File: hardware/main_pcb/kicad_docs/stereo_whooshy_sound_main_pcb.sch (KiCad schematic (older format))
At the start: 4 parts, among them J10 audio_in_B, J11 audio_out_A, J12 audio_out_B, J9 audio_in_A

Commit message: progress on schemo
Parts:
- removed J10: audio_in_B, Connector_PinHeader_2.54mm:PinHeader_1x02_P2.54mm_Vertical, symbol Connector_Generic:Conn_01x02
- removed J11: audio_out_A, Connector_PinHeader_2.54mm:PinHeader_1x02_P2.54mm_Vertical, symbol Connector_Generic:Conn_01x02
- removed J12: audio_out_B, Connector_PinHeader_2.54mm:PinHeader_1x02_P2.54mm_Vertical, symbol Connector_Generic:Conn_01x02
- removed J9: audio_in_A, Connector_PinHeader_2.54mm:PinHeader_1x02_P2.54mm_Vertical, symbol Connector_Generic:Conn_01x02
- added J10: IO_B, Connector_PinHeader_2.54mm:PinHeader_1x03_P2.54mm_Vertical, symbol Connector_Generic:Conn_01x03
- added J9: IO_A, Connector_PinHeader_2.54mm:PinHeader_1x03_P2.54mm_Vertical, symbol Connector_Generic:Conn_01x03
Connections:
- new net audio_in_A: J9.1 (Pin_1)
- new net audio_in_B: J10.1 (Pin_1)
- new net audio_out_A: J9.2 (Pin_2)
- new net audio_out_B: J10.2 (Pin_2)
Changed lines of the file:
@@
 $EndSheet
 $Comp
-L Connector_Generic:Conn_01x02 J9
-U 1 1 5FB8912F
-P 750 1650
-F 0 "J9" H 668 1867 50  0000 C CNN
-F 1 "audio_in_A" H 668 1776 50  0000 C CNN
-F 2 "Connector_PinHeader_2.54mm:PinHeader_1x02_P2.54mm_Vertical" H 750 1650 50  0001 C CNN
-F 3 "~" H 750 1650 50  0001 C CNN
-	1    750  1650
+L Connector_Generic:Conn_01x03 J9
+U 1 1 5FBA986C
+P 850 1150
+F 0 "J9" H 768 1467 50  0000 C CNN
+F 1 "IO_A" H 768 1376 50  0000 C CNN
+F 2 "Connector_PinHeader_2.54mm:PinHeader_1x03_P2.54mm_Vertical" H 850 1150 50  0001 C CNN
+F 3 "~" H 850 1150 50  0001 C CNN
+	1    850  1150
 	-1   0    0    -1
 $EndComp
 $Comp
-L Connector_Generic:Conn_01x02 J10
-U 1 1 5FB89C6A
-P 750 2400
-F 0 "J10" H 668 2617 50  0000 C CNN
-F 1 "audio_in_B" H 668 2526 50  0000 C CNN
-F 2 "Connector_PinHeader_2.54mm:PinHeader_1x02_P2.54mm_Vertical" H 750 2400 50  0001 C CNN
-F 3 "~" H 750 2400 50  0001 C CNN
-	1    750  2400
+L Connector_Generic:Conn_01x03 J10
+U 1 1 5FBA9F9C
+P 850 2000
+F 0 "J10" H 768 2317 50  0000 C CNN
+F 1 "IO_B" H 768 2226 50  0000 C CNN
+F 2 "Connector_PinHeader_2.54mm:PinHeader_1x03_P2.54mm_Vertical" H 850 2000 50  0001 C CNN
+F 3 "~" H 850 2000 50  0001 C CNN
+	1    850  2000
 	-1   0    0    -1
 $EndComp
-$Comp
-L power:GND #PWR01
-U 1 1 5FB8A139
-P 1050 1850
-F 0 "#PWR01" H 1050 1600 50  0001 C CNN
-F 1 "GND" H 1055 1677 50  0000 C CNN
-F 2 "" H 1050 1850 50  0001 C CNN
-F 3 "" H 1050 1850 50  0001 C CNN
-	1    1050 1850
-	1    0    0    -1
-$EndComp
-Wire Wire Line
-	1050 1850 1050 1750
-Wire Wire Line
-	1050 1750 950  1750
-$Comp
-L power:GND #PWR02
-U 1 1 5FB8AD56
-P 1050 2600
-F 0 "#PWR02" H 1050 2350 50  0001 C CNN
-F 1 "GND" H 1055 2427 50  0000 C CNN
-F 2 "" H 1050 2600 50  0001 C CNN
-F 3 "" H 1050 2600 50  0001 C CNN
-	1    1050 2600
-	1    0    0    -1
-$EndComp
-Wire Wire Line
-	1050 2600 1050 2500
-Wire Wire Line
-	1050 2500 950  2500
-$Comp
-L Connector_Generic:Conn_01x02 J11
-U 1 1 5FB8D888
-P 11000 1650
-F 0 "J11" H 10950 1900 50  0000 L CNN
-F 1 "audio_out_A" H 10750 1800 50  0000 L CNN
-F 2 "Connector_PinHeader_2.54mm:PinHeader_1x02_P2.54mm_Vertical" H 11000 1650 50  0001 C CNN
-F 3 "~" H 11000 1650 50  0001 C CNN
-	1    11000 1650
-	1    0    0    -1
-$EndComp
-$Comp
-L Connector_Generic:Conn_01x02 J12
-U 1 1 5FB8D88E
-P 11000 2400
-F 0 "J12" H 10950 2650 50  0000 L CNN
-F 1 "audio_out_B" H 10750 2550 50  0000 L CNN
-F 2 "Connector_PinHeader_2.54mm:PinHeader_1x02_P2.54mm_Vertical" H 11000 2400 50  0001 C CNN
-F 3 "~" H 11000 2400 50  0001 C CNN
-	1    11000 2400
-	1    0    0    -1
-$EndComp
-$Comp
-L power:GND #PWR021
-U 1 1 5FB8D894
-P 10700 1850
-F 0 "#PWR021" H 10700 1600 50  0001 C CNN
-F 1 "GND" H 10705 1677 50  0000 C CNN
-F 2 "" H 10700 1850 50  0001 C CNN
-F 3 "" H 10700 1850 50  0001 C CNN
-	1    10700 1850
-	-1   0    0    -1
-$EndComp
-Wire Wire Line
-	10700 1850 10700 1750
-Wire Wire Line
-	10700 1750 10800 1750
-$Comp
-L power:GND #PWR022
-U 1 1 5FB8D89C
-P 10700 2600
-F 0 "#PWR022" H 10700 2350 50  0001 C CNN
-F 1 "GND" H 10705 2427 50  0000 C CNN
-F 2 "" H 10700 2600 50  0001 C CNN
-F 3 "" H 10700 2600 50  0001 C CNN
-	1    10700 2600
-	-1   0    0    -1
-$EndComp
-Wire Wire Line
-	10700 2600 10700 2500
-Wire Wire Line
-	10700 2500 10800 2500
+Text Label 1050 1050 0    50   ~ 0
+audio_in_A
+Text Label 1050 1150 0    50   ~ 0
+audio_out_A
+Text Label 1050 1900 0    50   ~ 0
+audio_in_B
+Text Label 1050 2000 0    50   ~ 0
+audio_out_B
 $EndSCHEMATC

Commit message: progress on pcb layout
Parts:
- removed J10: IO_B, Connector_PinHeader_2.54mm:PinHeader_1x03_P2.54mm_Vertical, symbol Connector_Generic:Conn_01x03
- removed J9: IO_A, Connector_PinHeader_2.54mm:PinHeader_1x03_P2.54mm_Vertical, symbol Connector_Generic:Conn_01x03
- added J1, J2, J3, J4, J5, J6: NRJ6HM-1, Connector_Audio:Jack_6.35mm_Neutrik_NRJ6HM-1_Horizontal, symbol Connector:AudioJack3_Switch
- added J16: Jack-DC, Connector_BarrelJack:BarrelJack_CUI_PJ-063AH_Horizontal, symbol Connector:Jack-DC
- added J17: footswitch_A, Connector_PinHeader_2.54mm:PinHeader_1x02_P2.54mm_Vertical, symbol Connector_Generic:Conn_01x02
- added J18: footswitch_B, Connector_PinHeader_2.54mm:PinHeader_1x02_P2.54mm_Vertical, symbol Connector_Generic:Conn_01x02
- added R51, R52: 10k, Resistor_SMD:R_0603_1608Metric, symbol Device:R
- added R53, R54: 1M, Resistor_SMD:R_0603_1608Metric, symbol Device:R
- added SW1: SW_DP_on_on_on, custom_footprints:DPDT_mini_toggle, symbol custom_components:SW_DP_on_on_on
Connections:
- new net: SW1.2 (B), SW1.4 (A)
- new net: J18.1 (Pin_1), R52.2
- new net: J17.1 (Pin_1), R51.2
- new net +9V: R51.1, R52.1
- new net GND: J1.S, J1.TN, J2.S, J3.S, J3.TN, J4.S, J5.S, J5.TN, J6.S, J6.TN, R53.2, R54.2
- new net audio_input_buffers/dry_in_A: J1.T
- new net audio_input_buffers/dry_in_B: J3.T
- new net audio_output_buffers/final_out_A: J2.T
- new net audio_output_buffers/final_out_B: J4.T
- new net bypass_switches/bypass_logic_in_A: J17.2 (Pin_2), R53.1
- new net bypass_switches/bypass_logic_in_B: J18.2 (Pin_2), R54.1
- new net control_voltage_generators/exp_ped_ring_current_A: J5.R
- new net control_voltage_generators/exp_ped_ring_current_B: J6.R
- new net control_voltage_generators/ext_cv_A: J5.T
- new net control_voltage_generators/ext_cv_B: J6.T
- new net dry_A: SW1.6 (C)
- new net dry_B: SW1.1 (A)
- new net power_supply/9VDC_in: J16.2
- new net power_supply/power_gnd_in: J16.1
- new net switched_dry_B: SW1.5 (B)
- new net wet_A: SW1.3 (C)
- no-connect marks 0 -> 18

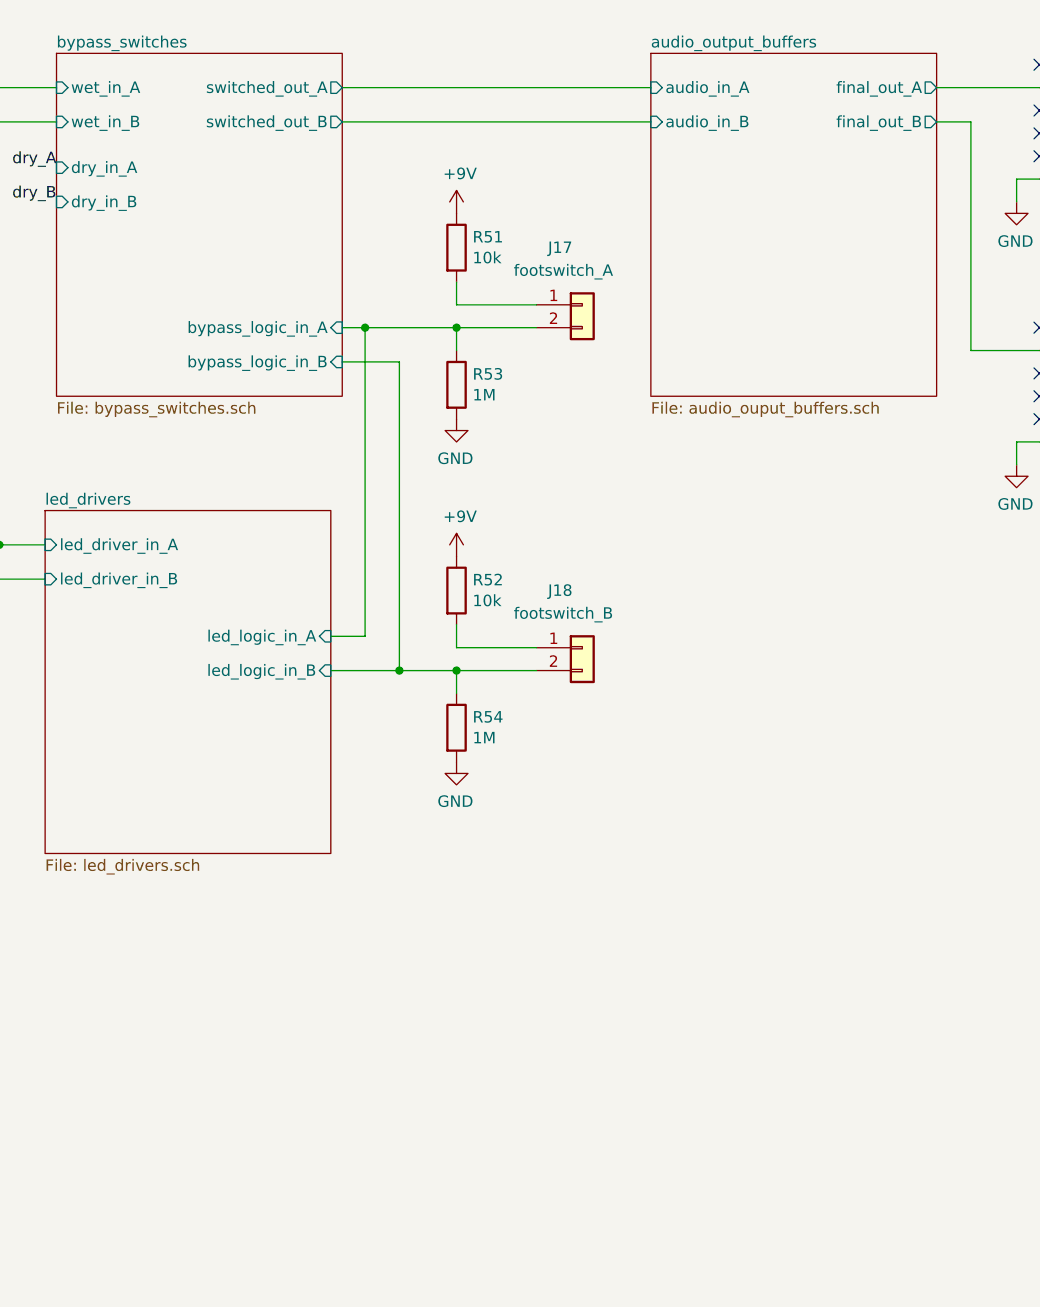
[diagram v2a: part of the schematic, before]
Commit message: reduce analog switch count, tidy up
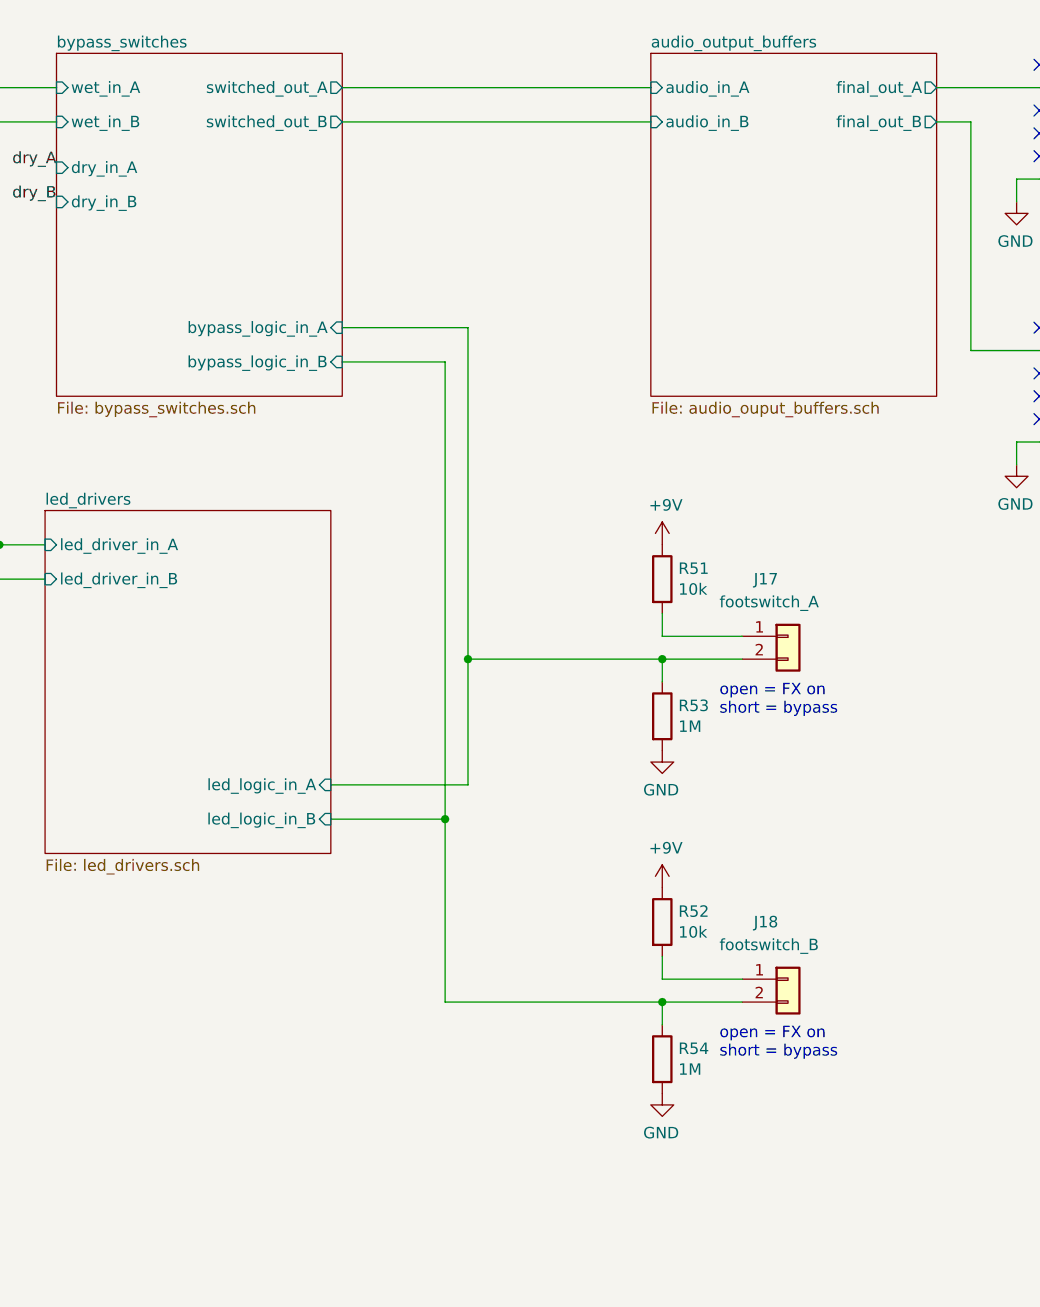
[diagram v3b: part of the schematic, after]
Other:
- note added: "open = FX on\nshort = bypass"
- moved on the sheet: J17, J18, R51, R52, R53, R54
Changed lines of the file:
@@
 F2 "led_driver_in_A" I L 6200 3650 50
 F3 "led_driver_in_B" I L 6200 3800 50
-F4 "led_logic_in_A" I R 7450 4050 50
-F5 "led_logic_in_B" I R 7450 4200 50
+F4 "led_logic_in_A" I R 7450 4700 50
+F5 "led_logic_in_B" I R 7450 4850 50
 $EndSheet
 $Sheet
@@
 L Connector_Generic:Conn_01x02 J18
 U 1 1 613612C4
-P 8550 4100
-F 0 "J18" H 8400 4350 50  0000 L CNN
-F 1 "footswitch_B" H 8250 4250 50  0000 L CNN
-F 2 "Connector_PinHeader_2.54mm:PinHeader_1x02_P2.54mm_Vertical" H 8550 4100 50  0001 C CNN
-F 3 "~" H 8550 4100 50  0001 C CNN
-	1    8550 4100
-	1    0    0    -1
-$EndComp
-Wire Wire Line
-	7500 2850 7750 2850
+P 9450 5550
+F 0 "J18" H 9300 5800 50  0000 L CNN
+F 1 "footswitch_B" H 9150 5700 50  0000 L CNN
+F 2 "Connector_PinHeader_2.54mm:PinHeader_1x02_P2.54mm_Vertical" H 9450 5550 50  0001 C CNN
+F 3 "~" H 9450 5550 50  0001 C CNN
+	1    9450 5550
+	1    0    0    -1
+$EndComp
 $Comp
 L Connector_Generic:Conn_01x02 J17
 U 1 1 6136C681
-P 8550 2600
-F 0 "J17" H 8400 2850 50  0000 L CNN
-F 1 "footswitch_A" H 8250 2750 50  0000 L CNN
-F 2 "Connector_PinHeader_2.54mm:PinHeader_1x02_P2.54mm_Vertical" H 8550 2600 50  0001 C CNN
-F 3 "~" H 8550 2600 50  0001 C CNN
-	1    8550 2600
-	1    0    0    -1
-$EndComp
-Wire Wire Line
-	7500 2700 7600 2700
+P 9450 4050
+F 0 "J17" H 9300 4300 50  0000 L CNN
+F 1 "footswitch_A" H 9150 4200 50  0000 L CNN
+F 2 "Connector_PinHeader_2.54mm:PinHeader_1x02_P2.54mm_Vertical" H 9450 4050 50  0001 C CNN
+F 3 "~" H 9450 4050 50  0001 C CNN
+	1    9450 4050
+	1    0    0    -1
+$EndComp
 Text Label 4250 2200 2    50   ~ 0
 switched_dry_B
@@
 Wire Wire Line
 	2750 1650 4250 1650
-Wire Wire Line
-	7450 4050 7600 4050
-Wire Wire Line
-	7450 4200 7750 4200
 $Comp
 L Device:R R52
 U 1 1 6141E931
-P 8000 3850
-F 0 "R52" H 8070 3896 50  0000 L CNN
-F 1 "10k" H 8070 3805 50  0000 L CNN
-F 2 "Resistor_SMD:R_0603_1608Metric" V 7930 3850 50  0001 C CNN
-F 3 "~" H 8000 3850 50  0001 C CNN
-	1    8000 3850
+P 8900 5300
+F 0 "R52" H 8970 5346 50  0000 L CNN
+F 1 "10k" H 8970 5255 50  0000 L CNN
+F 2 "Resistor_SMD:R_0603_1608Metric" V 8830 5300 50  0001 C CNN
+F 3 "~" H 8900 5300 50  0001 C CNN
+	1    8900 5300
 	1    0    0    -1
 $EndComp
@@
 L Device:R R51
 U 1 1 6141F133
-P 8000 2350
-F 0 "R51" H 8070 2396 50  0000 L CNN
-F 1 "10k" H 8070 2305 50  0000 L CNN
-F 2 "Resistor_SMD:R_0603_1608Metric" V 7930 2350 50  0001 C CNN
-F 3 "~" H 8000 2350 50  0001 C CNN
-	1    8000 2350
-	1    0    0    -1
-$EndComp
-Wire Wire Line
-	7600 2700 7600 4050
-Wire Wire Line
-	8350 2600 8000 2600
-Wire Wire Line
-	8000 2600 8000 2500
-Wire Wire Line
-	8350 2700 8000 2700
-Connection ~ 7600 2700
-Wire Wire Line
-	8350 4100 8000 4100
-Wire Wire Line
-	8000 4100 8000 4000
-Wire Wire Line
-	8350 4200 8000 4200
+P 8900 3800
+F 0 "R51" H 8970 3846 50  0000 L CNN
+F 1 "10k" H 8970 3755 50  0000 L CNN
+F 2 "Resistor_SMD:R_0603_1608Metric" V 8830 3800 50  0001 C CNN
+F 3 "~" H 8900 3800 50  0001 C CNN
+	1    8900 3800
+	1    0    0    -1
+$EndComp
+Wire Wire Line
+	9250 4050 8900 4050
+Wire Wire Line
+	8900 4050 8900 3950
+Wire Wire Line
+	9250 5550 8900 5550
+Wire Wire Line
+	8900 5550 8900 5450
+Wire Wire Line
+	9250 5650 8900 5650
 Text Label 5500 1650 0    50   ~ 0
 wet_A
@@
 L power:+9V #PWR01
 U 1 1 610E86B7
-P 8000 2200
-F 0 "#PWR01" H 8000 2050 50  0001 C CNN
-F 1 "+9V" H 8015 2373 50  0000 C CNN
-F 2 "" H 8000 2200 50  0001 C CNN
-F 3 "" H 8000 2200 50  0001 C CNN
-	1    8000 2200
+P 8900 3650
+F 0 "#PWR01" H 8900 3500 50  0001 C CNN
+F 1 "+9V" H 8915 3823 50  0000 C CNN
+F 2 "" H 8900 3650 50  0001 C CNN
+F 3 "" H 8900 3650 50  0001 C CNN
+	1    8900 3650
 	1    0    0    -1
 $EndComp
@@
 L power:+9V #PWR029
 U 1 1 610E8AAF
-P 8000 3700
-F 0 "#PWR029" H 8000 3550 50  0001 C CNN
-F 1 "+9V" H 8015 3873 50  0000 C CNN
-F 2 "" H 8000 3700 50  0001 C CNN
-F 3 "" H 8000 3700 50  0001 C CNN
-	1    8000 3700
-	1    0    0    -1
-$EndComp
-Connection ~ 7750 4200
-Wire Wire Line
-	7750 2850 7750 4200
+P 8900 5150
+F 0 "#PWR029" H 8900 5000 50  0001 C CNN
+F 1 "+9V" H 8915 5323 50  0000 C CNN
+F 2 "" H 8900 5150 50  0001 C CNN
+F 3 "" H 8900 5150 50  0001 C CNN
+	1    8900 5150
+	1    0    0    -1
+$EndComp
 $Comp
 L Device:R R53
 U 1 1 61102F6A
-P 8000 2950
-F 0 "R53" H 8070 2996 50  0000 L CNN
-F 1 "1M" H 8070 2905 50  0000 L CNN
-F 2 "Resistor_SMD:R_0603_1608Metric" V 7930 2950 50  0001 C CNN
-F 3 "~" H 8000 2950 50  0001 C CNN
-	1    8000 2950
+P 8900 4400
+F 0 "R53" H 8970 4446 50  0000 L CNN
+F 1 "1M" H 8970 4355 50  0000 L CNN
+F 2 "Resistor_SMD:R_0603_1608Metric" V 8830 4400 50  0001 C CNN
+F 3 "~" H 8900 4400 50  0001 C CNN
+	1    8900 4400
 	1    0    0    -1
 $EndComp
@@
 L power:GND #PWR?
 U 1 1 611033F5
-P 8000 3100
+P 8900 4550
 AR Path="/5FB7EF95/611033F5" Ref="#PWR?"  Part="1"
 AR Path="/611033F5" Ref="#PWR02"  Part="1"
-F 0 "#PWR02" H 8000 2850 50  0001 C CNN
-F 1 "GND" H 8005 2927 50  0000 C CNN
-F 2 "" H 8000 3100 50  0001 C CNN
-F 3 "" H 8000 3100 50  0001 C CNN
-	1    8000 3100
+F 0 "#PWR02" H 8900 4300 50  0001 C CNN
+F 1 "GND" H 8905 4377 50  0000 C CNN
+F 2 "" H 8900 4550 50  0001 C CNN
+F 3 "" H 8900 4550 50  0001 C CNN
+	1    8900 4550
 	-1   0    0    -1
 $EndComp
 Wire Wire Line
-	8000 2800 8000 2700
-Connection ~ 8000 2700
-Wire Wire Line
-	8000 2700 7600 2700
+	8900 4250 8900 4150
 $Comp
 L Device:R R54
 U 1 1 6110736F
-P 8000 4450
-F 0 "R54" H 8070 4496 50  0000 L CNN
-F 1 "1M" H 8070 4405 50  0000 L CNN
-F 2 "Resistor_SMD:R_0603_1608Metric" V 7930 4450 50  0001 C CNN
-F 3 "~" H 8000 4450 50  0001 C CNN
-	1    8000 4450
+P 8900 5900
+F 0 "R54" H 8970 5946 50  0000 L CNN
+F 1 "1M" H 8970 5855 50  0000 L CNN
+F 2 "Resistor_SMD:R_0603_1608Metric" V 8830 5900 50  0001 C CNN
+F 3 "~" H 8900 5900 50  0001 C CNN
+	1    8900 5900
 	1    0    0    -1
 $EndComp
@@
 L power:GND #PWR?
 U 1 1 61107375
-P 8000 4600
+P 8900 6050
 AR Path="/5FB7EF95/61107375" Ref="#PWR?"  Part="1"
 AR Path="/61107375" Ref="#PWR030"  Part="1"
-F 0 "#PWR030" H 8000 4350 50  0001 C CNN
-F 1 "GND" H 8005 4427 50  0000 C CNN
-F 2 "" H 8000 4600 50  0001 C CNN
-F 3 "" H 8000 4600 50  0001 C CNN
-	1    8000 4600
+F 0 "#PWR030" H 8900 5800 50  0001 C CNN
+F 1 "GND" H 8905 5877 50  0000 C CNN
+F 2 "" H 8900 6050 50  0001 C CNN
+F 3 "" H 8900 6050 50  0001 C CNN
+	1    8900 6050
 	-1   0    0    -1
 $EndComp
 Wire Wire Line
-	8000 4300 8000 4200
-Connection ~ 8000 4200
-Wire Wire Line
-	8000 4200 7750 4200
+	8900 5750 8900 5650
 $Comp
 L custom_components:SW_DP_on_on_on SW1
@@
 Text Label 3300 3200 2    50   ~ 0
 dry_B
+Text Notes 9150 4400 0    50   ~ 0
+open = FX on\nshort = bypass
+Text Notes 9150 5900 0    50   ~ 0
+open = FX on\nshort = bypass
+Wire Wire Line
+	7450 4850 7950 4850
+Wire Wire Line
+	7950 4850 7950 5650
+Wire Wire Line
+	7950 5650 8900 5650
+Connection ~ 8900 5650
+Wire Wire Line
+	7450 4700 8050 4700
+Wire Wire Line
+	8050 4700 8050 4150
+Wire Wire Line
+	8050 4150 8900 4150
+Connection ~ 8900 4150
+Wire Wire Line
+	8900 4150 9250 4150
+Wire Wire Line
+	7950 4850 7950 2850
+Wire Wire Line
+	7950 2850 7500 2850
+Connection ~ 7950 4850
+Wire Wire Line
+	8050 4150 8050 2700
+Wire Wire Line
+	8050 2700 7500 2700
+Connection ~ 8050 4150
 $EndSCHEMATC
